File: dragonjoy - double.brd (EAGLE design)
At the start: 53.3 x 69.5 mm, 24 parts, among them IC1 4066N, IC2 4066N

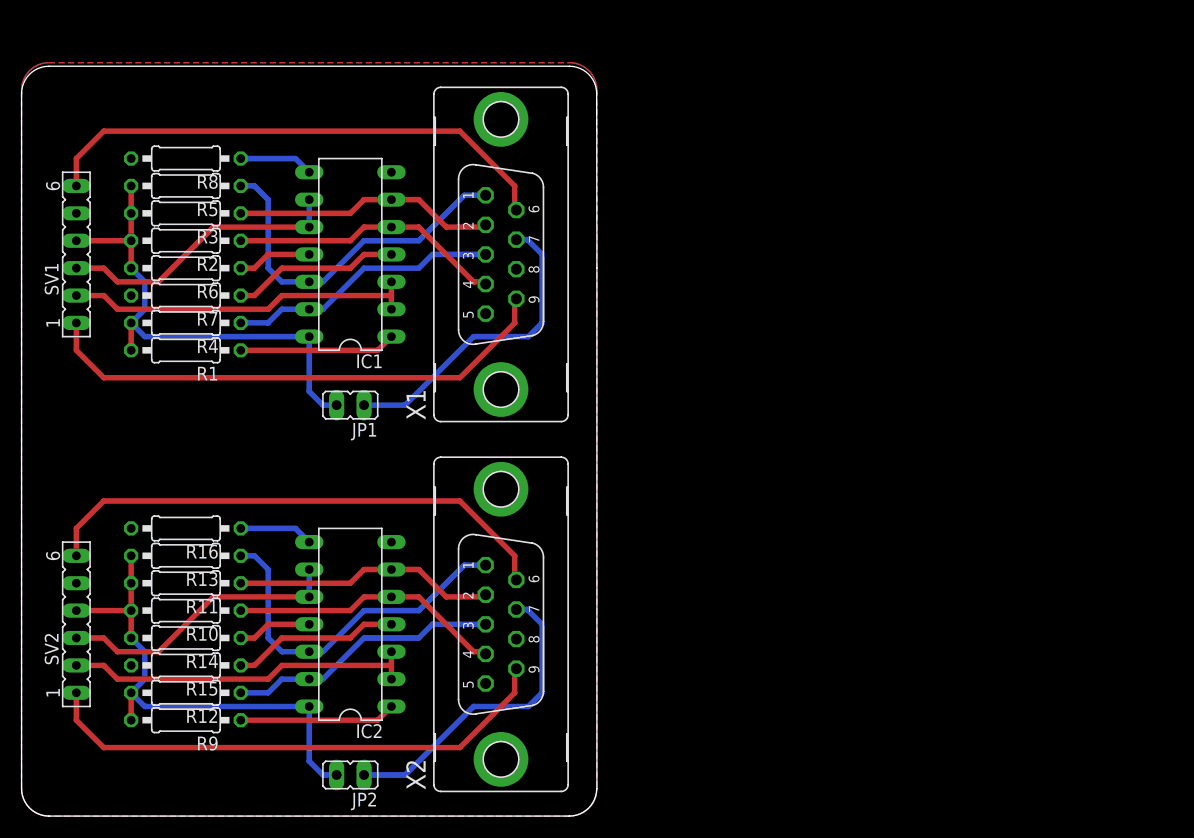
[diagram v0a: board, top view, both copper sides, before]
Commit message: update double board for printing and etching
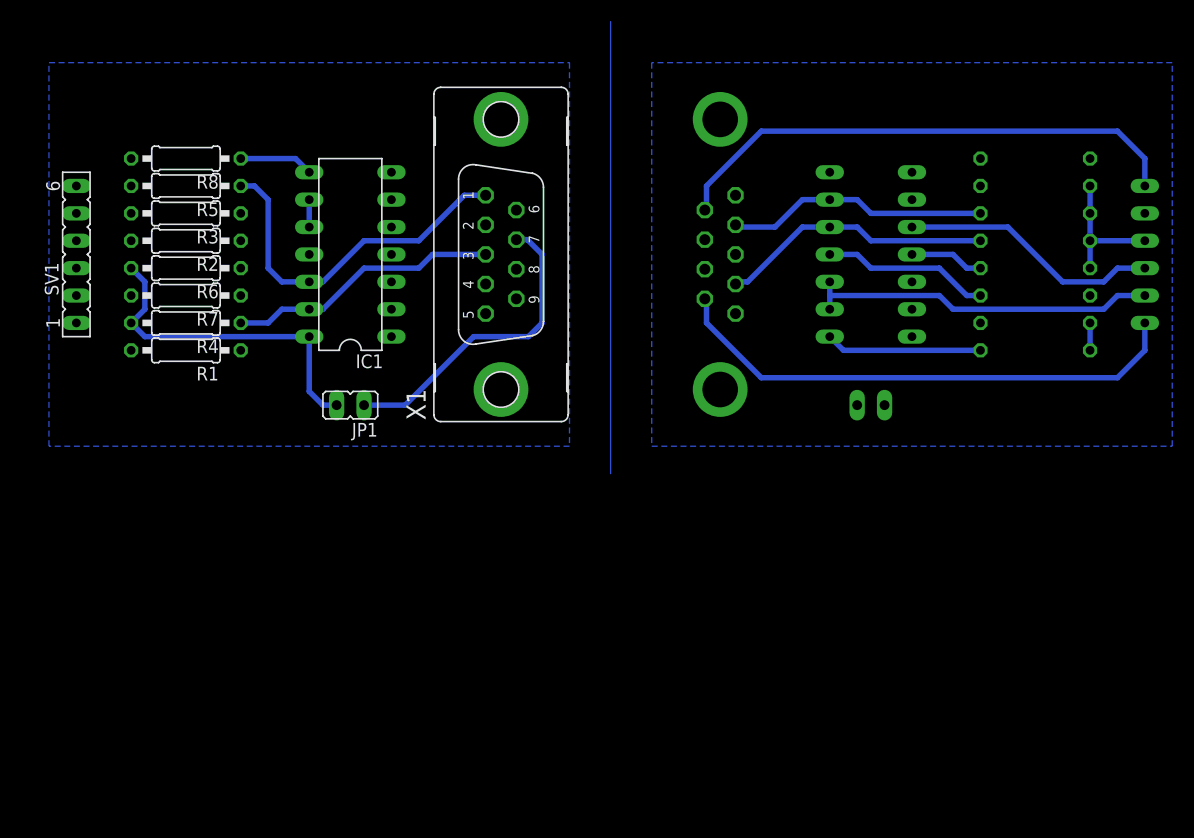
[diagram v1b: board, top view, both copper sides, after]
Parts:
- removed IC2: 4066N, 40xx:DIL14
- removed JP2: (no value), jumper:JP1
- removed R10, R11, R12, R13, R14, R15, R16, R9: (no value), rcl:0207/10
- removed SV2: (no value), con-lsta:FE06
- removed X2: (no value), con-subd:F09VP
- added IC3: 4066N, 40xx:DIL14
- added JP3: (no value), jumper:JP1
- added R17, R18, R19, R20, R21, R22, R23, R24: (no value), rcl:0207/10
- added SV3: (no value), con-lsta:FE06
- added X3: (no value), con-subd:F09VP
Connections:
- removed net DN: IC1.6, R3.1, X1.2
- removed net DN1: IC2.6, R11.1, X2.2
- removed net FIRE: SV1.6, X1.6
- removed net FIRE1: SV2.6, X2.6
- removed net FIRE2: SV1.1, X1.9
- removed net FIRE3: SV2.1, X2.9
- removed net LT1: IC2.13, R12.1, X2.3
- removed net N$2: IC2.1, R9.1
- removed net N$3: IC1.1, R1.1
- removed net N$4: IC2.11, R14.1
- removed net N$5: IC2.4, R15.1
- removed net N$6: IC2.8, R16.1
- removed net N$7: JP2.1, X2.7
- removed net N$8: IC1.11, R6.1
- removed net N$9: IC1.4, R7.1
- removed net RT: IC1.5, R2.1, X1.4
- removed net RT1: IC2.5, R10.1, X2.4
- removed net UP1: IC2.12, R13.1, X2.1
- removed net VCC1: IC2.14, JP2.2, R10.2, R11.2, R12.2, R13.2, R14.2, R9.2, SV2.4
- removed net X: IC1.2, IC1.3, SV1.2
- removed net X1: IC2.2, IC2.3, SV2.2
- removed net Y1: IC2.10, IC2.9, SV2.3
- new net DN2: IC3.6, R19.1, X3.2
- new net FIRE4: SV3.6, X3.6
- new net FIRE5: SV3.1, X3.9
- new net GND2: IC3.7, R23.2, R24.2, SV3.5, X3.8
- new net N$11: IC3.1, R17.1
- new net N$12: IC3.11, R22.1
- new net N$13: IC3.4, R23.1
- new net RT2: IC3.5, R18.1, X3.4
- new net S$2: R18.2, R19.2, R21.2, R22.2, SV3.4
- new net VCC2: R17.2, R20.2
- new net X2: IC3.2, IC3.3, SV3.2
- new net Y2: IC3.10, SV3.3
- net GND: no longer IC2.7, R15.2, R16.2, SV2.5, X2.8
- net VCC: no longer R1.2, R2.2, R3.2, R5.2, SV1.4
- net Y: no longer SV1.3
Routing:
- net FIRE2: track 48.6 -> 0.00 mm
- net FIRE5: track 0.00 -> 48.6 mm
- net FIRE1: track 48.6 -> 0.00 mm
- net FIRE3: track 48.6 -> 0.00 mm
- net FIRE: track 48.6 -> 0.00 mm
- net FIRE4: track 0.00 -> 48.6 mm
- net VCC1: track 46.6 -> 0.00 mm
- net S$1: track 0.00 -> 41.9 mm
- net UP1: track 33.4 -> 0.00 mm
- net X2: track 0.00 -> 32.8 mm
- net X1: track 32.8 -> 0.00 mm
- net X: track 32.8 -> 0.00 mm
- net N$7: track 29.0 -> 0.00 mm
- net Y1: track 26.8 -> 0.00 mm
- net RT2: track 0.00 -> 25.8 mm
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- added copper zone on layer 16, net GND2
- removed copper zone on layer 1, net GND
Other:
- board outline removed
